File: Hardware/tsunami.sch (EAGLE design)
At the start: 157 parts, among them J1 VDC-IN, J10 TRIG2, J11 TRIG1, J12 USD-SDIO-SOCKET, J13 GND, J14 AUDIO I/O, J15 MIDI, J2 GND-IN, J3 DEBUG, J4 USB-MICROB", J5 CORTEX_DEBUGPTH, J6 3.3VA, J7 3.3V, J8 PLAYING, J9 FTDI_DEVICE, Q1 2.5A/30V, U1 LM1117, U2 LM1117, U3 ATSAMS70N20A-AN, U4 AK4618VQSFE-PACKAGE, U5 74AHC1G125, U6 6N138M, Y1 11.2896 MHz

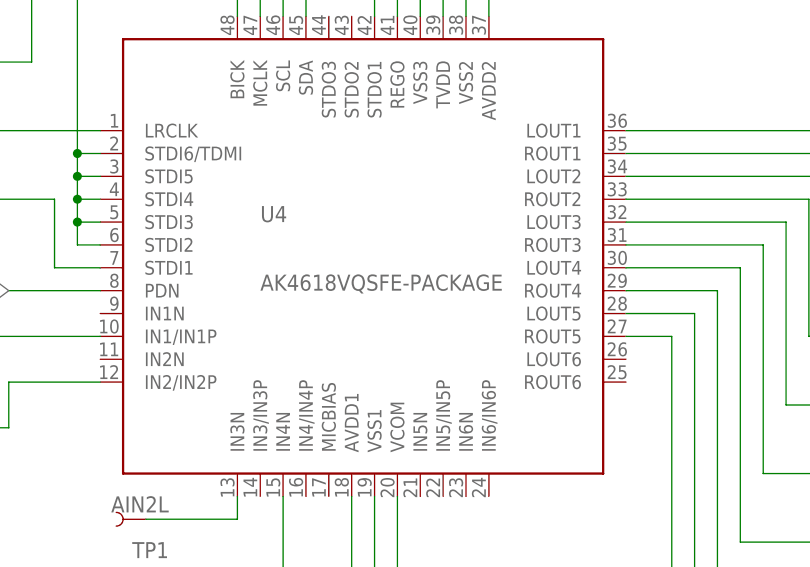
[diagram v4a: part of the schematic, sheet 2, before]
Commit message: Post review & production checklist.
-Centered staking vias on USB.
-Moved some vias to avoid silk.
-Text touchups around V reg outputs.
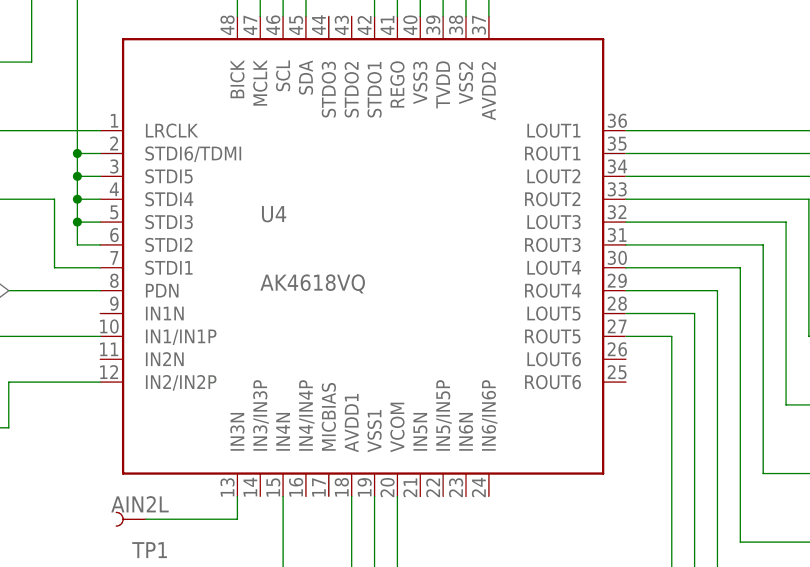
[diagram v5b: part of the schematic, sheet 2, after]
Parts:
- U4: value AK4618VQSFE-PACKAGE -> AK4618VQ
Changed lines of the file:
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@@
 <part name="Y1" library="tapestry" deviceset="CRYSTAL-11.2896" device="" value="11.2896 MHz"/>
 <part name="GND16" library="SparkFun-Aesthetics" deviceset="GND" device=""/>
-<part name="U4" library="tapestry" deviceset="AK4618VQ" device="SFE-PACKAGE" value="AK4618VQSFE-PACKAGE"/>
+<part name="U4" library="tapestry" deviceset="AK4618VQ" device="SFE-PACKAGE" value="AK4618VQ"/>
 <part name="GND45" library="SparkFun-Aesthetics" deviceset="GND" device=""/>
 <part name="C36" library="SparkFun-Capacitors" deviceset="1.0UF-16V-10%(0603)" device="" value="1.0uF"/>
